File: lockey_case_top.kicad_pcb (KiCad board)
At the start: 2 copper layers, 98.4 x 89.2 mm, 1 part

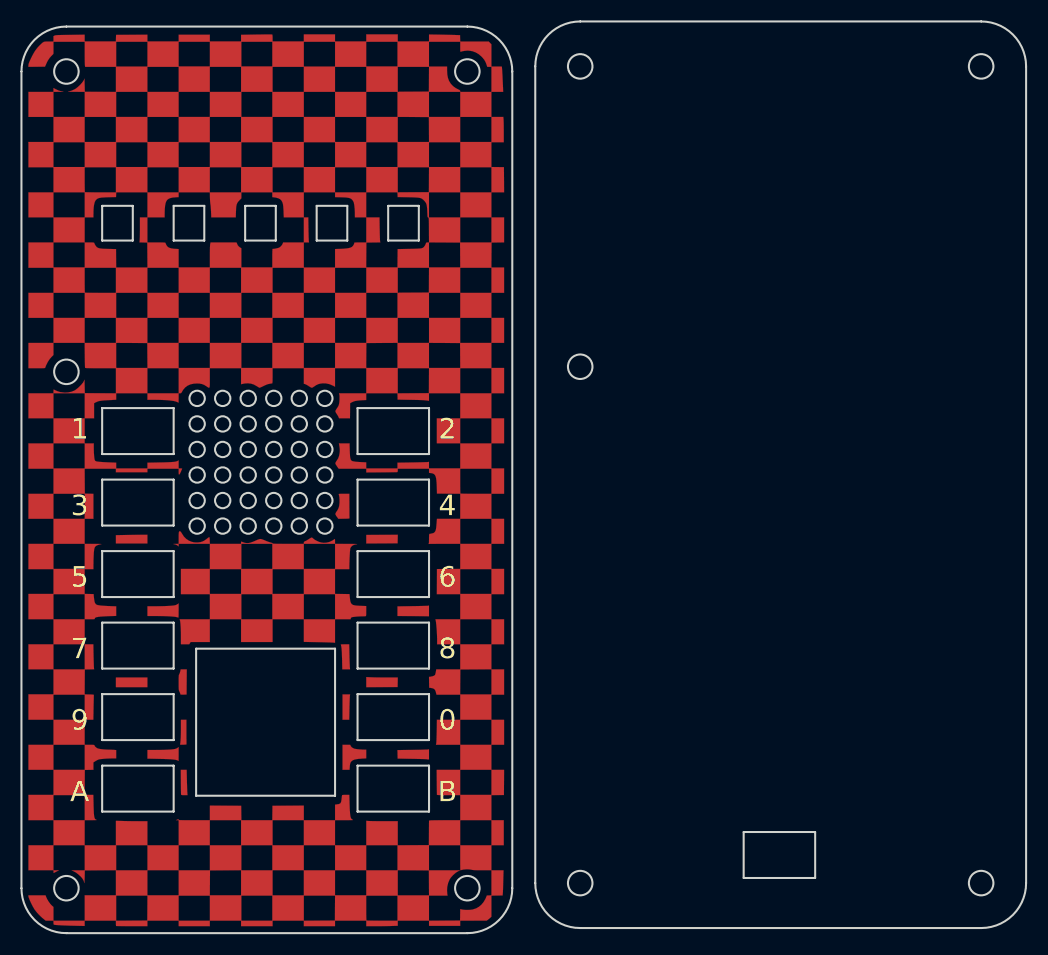
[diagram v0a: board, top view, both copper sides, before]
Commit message: :bug: (case) rename case pcb filename
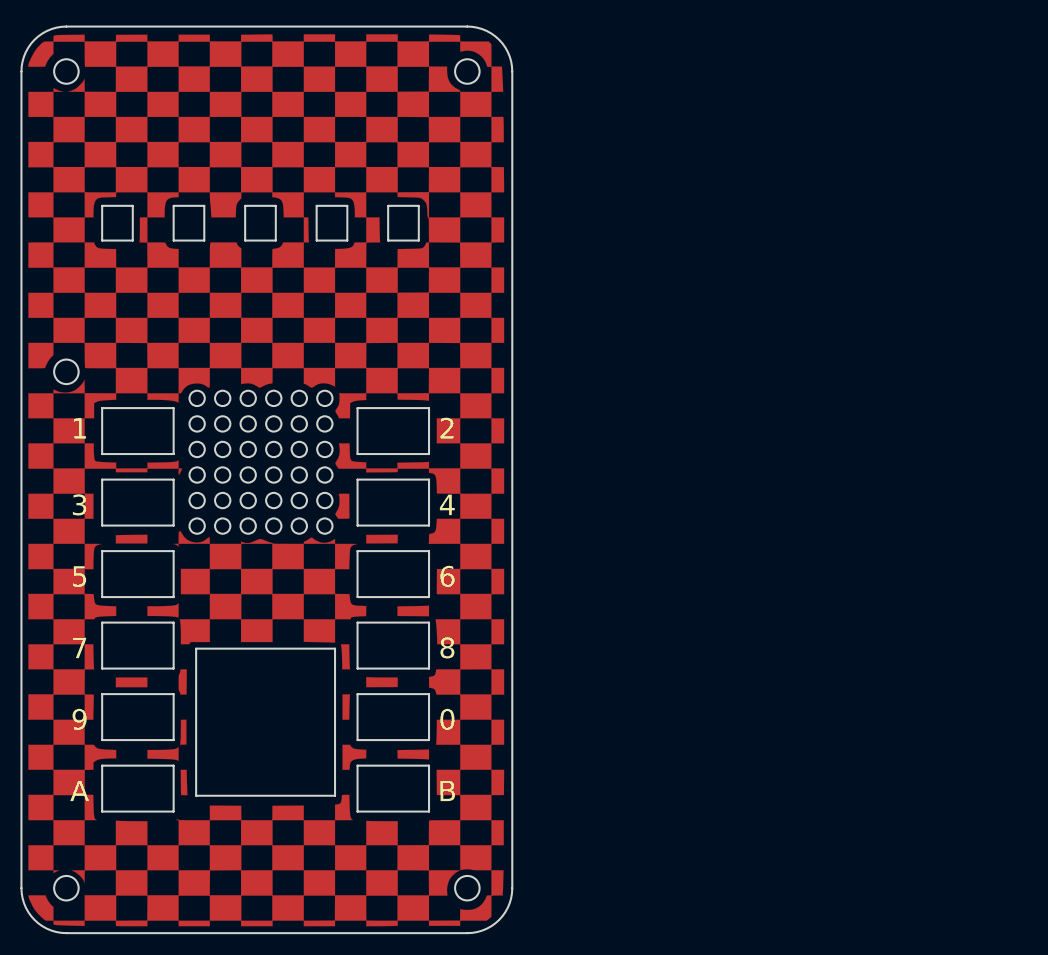
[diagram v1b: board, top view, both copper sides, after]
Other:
- board size 98.4 x 89.2 mm -> 48.1 x 88.8 mm
- board text removed: "RESET"
